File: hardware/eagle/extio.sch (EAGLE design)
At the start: 46 parts, among them IC1 PCF8574P, Q1 IRLZ44N, Q2 IRLZ44N, Q3 IRLZ44N, Q4 IRLZ44N, Q5 IRLZ44N, Q6 IRLZ44N, Q7 IRLZ44N, Q8 IRLZ44N

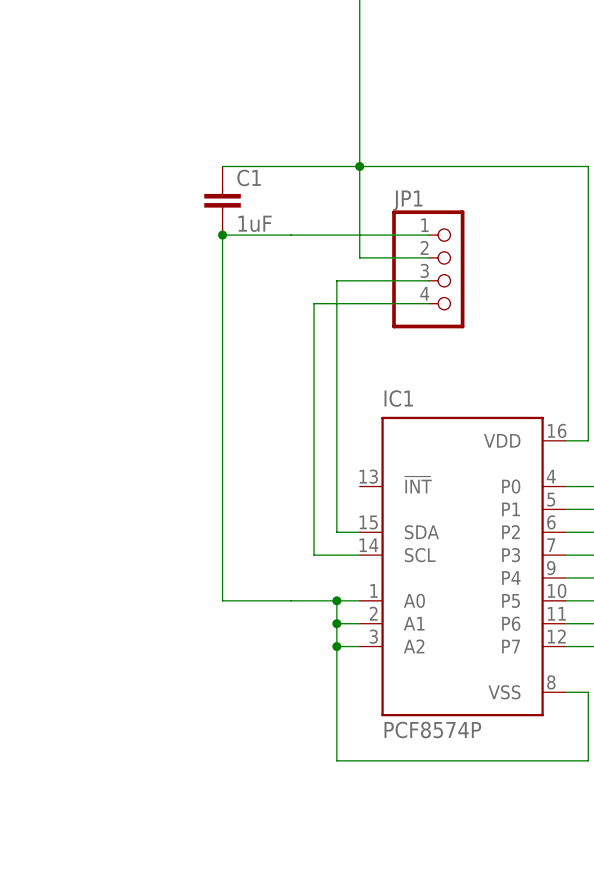
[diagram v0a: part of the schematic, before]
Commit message: ExtIO A0..A1: jmp1..jmp2
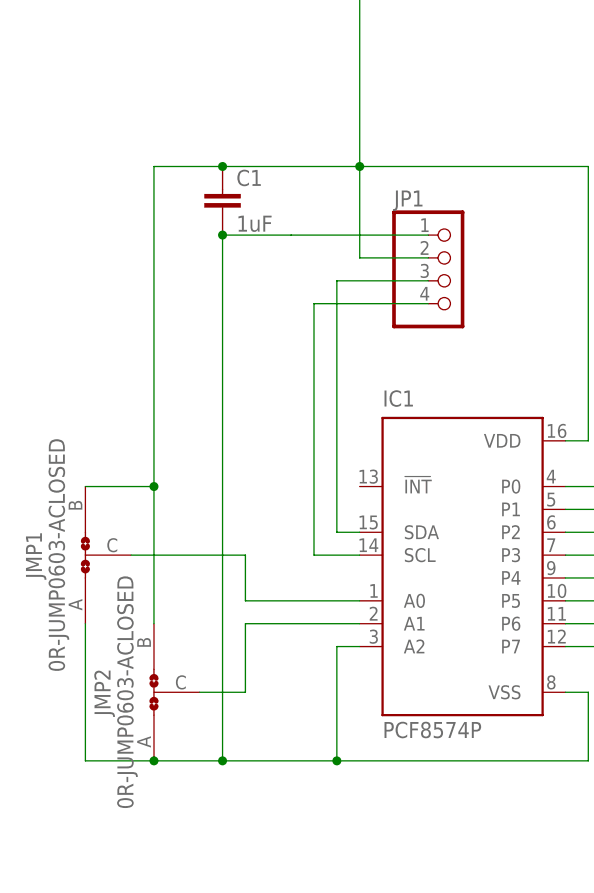
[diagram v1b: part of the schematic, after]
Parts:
- added JMP1, JMP2: 0R-JUMP0603-ACLOSED, gate433:0R-JUMP0603-ACLOSED
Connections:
- removed net N$71: C1.2, IC1.A0, IC1.A1, IC1.A2, IC1.VSS, JP1.1
- new net N$1: C1.2, IC1.A2, IC1.VSS, JMP1.A, JMP2.A, JP1.1
- new net N$2: IC1.A0, JMP1.C
- new net N$3: IC1.A1, JMP2.C
- net N$69: now also JMP1.B, JMP2.B
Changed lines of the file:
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@@
 <part name="D8" library="gate433" deviceset="ZENER-DIODE" device="SOD80C"/>
 <part name="C1" library="resistor" deviceset="C-EU" device="C0603" value="1uF"/>
+<part name="JMP1" library="gate433" deviceset="0R-JUMP" device="0603-ACLOSED"/>
+<part name="JMP2" library="gate433" deviceset="0R-JUMP" device="0603-ACLOSED"/>
 </parts>
 <sheets>
@@
 <instance part="D8" gate="G$1" x="170.18" y="17.78" rot="R90"/>
 <instance part="C1" gate="G$1" x="-5.08" y="83.82"/>
+<instance part="JMP1" gate="-0R" x="-20.32" y="43.18" rot="R90"/>
+<instance part="JMP2" gate="-0R" x="-12.7" y="27.94" rot="R90"/>
 </instances>
 <busses>
@@
 <pinref part="C1" gate="G$1" pin="1"/>
 <wire x1="-5.08" y1="86.36" x2="10.16" y2="86.36" width="0.1524" layer="91"/>
-</segment>
-</net>
-<net name="N$71" class="0">
-<segment>
-<pinref part="IC1" gate="G$1" pin="A0"/>
-<wire x1="10.16" y1="38.1" x2="7.62" y2="38.1" width="0.1524" layer="91"/>
-<wire x1="7.62" y1="38.1" x2="7.62" y2="35.56" width="0.1524" layer="91"/>
-<pinref part="IC1" gate="G$1" pin="A1"/>
-<wire x1="7.62" y1="35.56" x2="7.62" y2="33.02" width="0.1524" layer="91"/>
-<wire x1="10.16" y1="35.56" x2="7.62" y2="35.56" width="0.1524" layer="91"/>
-<junction x="7.62" y="35.56"/>
+<pinref part="JMP2" gate="-0R" pin="B"/>
+<wire x1="-12.7" y1="35.56" x2="-12.7" y2="50.8" width="0.1524" layer="91"/>
+<wire x1="-12.7" y1="50.8" x2="-12.7" y2="86.36" width="0.1524" layer="91"/>
+<wire x1="-12.7" y1="86.36" x2="-5.08" y2="86.36" width="0.1524" layer="91"/>
+<junction x="-5.08" y="86.36"/>
+<pinref part="JMP1" gate="-0R" pin="B"/>
+<wire x1="-20.32" y1="50.8" x2="-12.7" y2="50.8" width="0.1524" layer="91"/>
+<junction x="-12.7" y="50.8"/>
+</segment>
+</net>
+<net name="N$1" class="0">
+<segment>
+<pinref part="C1" gate="G$1" pin="2"/>
+<pinref part="JP1" gate="A" pin="1"/>
+<wire x1="2.54" y1="78.74" x2="17.78" y2="78.74" width="0.1524" layer="91"/>
+<wire x1="2.54" y1="78.74" x2="-5.08" y2="78.74" width="0.1524" layer="91"/>
 <pinref part="IC1" gate="G$1" pin="A2"/>
 <wire x1="10.16" y1="33.02" x2="7.62" y2="33.02" width="0.1524" layer="91"/>
@@
 <wire x1="35.56" y1="20.32" x2="7.62" y2="20.32" width="0.1524" layer="91"/>
 <wire x1="7.62" y1="20.32" x2="7.62" y2="33.02" width="0.1524" layer="91"/>
-<junction x="7.62" y="33.02"/>
-<wire x1="7.62" y1="38.1" x2="2.54" y2="38.1" width="0.1524" layer="91"/>
-<junction x="7.62" y="38.1"/>
-<pinref part="JP1" gate="A" pin="1"/>
-<wire x1="2.54" y1="78.74" x2="17.78" y2="78.74" width="0.1524" layer="91"/>
-<pinref part="C1" gate="G$1" pin="2"/>
-<wire x1="-5.08" y1="78.74" x2="-5.08" y2="38.1" width="0.1524" layer="91"/>
-<wire x1="-5.08" y1="38.1" x2="2.54" y2="38.1" width="0.1524" layer="91"/>
-<wire x1="2.54" y1="78.74" x2="-5.08" y2="78.74" width="0.1524" layer="91"/>
+<pinref part="JMP2" gate="-0R" pin="A"/>
+<wire x1="-12.7" y1="20.32" x2="-5.08" y2="20.32" width="0.1524" layer="91"/>
+<junction x="7.62" y="20.32"/>
+<pinref part="JMP1" gate="-0R" pin="A"/>
+<wire x1="-5.08" y1="20.32" x2="7.62" y2="20.32" width="0.1524" layer="91"/>
+<wire x1="-20.32" y1="35.56" x2="-20.32" y2="20.32" width="0.1524" layer="91"/>
+<wire x1="-20.32" y1="20.32" x2="-12.7" y2="20.32" width="0.1524" layer="91"/>
+<junction x="-12.7" y="20.32"/>
+<wire x1="-5.08" y1="78.74" x2="-5.08" y2="20.32" width="0.1524" layer="91"/>
 <junction x="-5.08" y="78.74"/>
-</segment>
-</net>
+<junction x="-5.08" y="20.32"/>
+</segment>
+</net>
+<net name="N$2" class="0">
+<segment>
+<pinref part="JMP1" gate="-0R" pin="C"/>
+<wire x1="-15.24" y1="43.18" x2="-2.54" y2="43.18" width="0.1524" layer="91"/>
+<wire x1="-2.54" y1="43.18" x2="-2.54" y2="38.1" width="0.1524" layer="91"/>
+<pinref part="IC1" gate="G$1" pin="A0"/>
+<wire x1="-2.54" y1="38.1" x2="10.16" y2="38.1" width="0.1524" layer="91"/>
+</segment>
+</net>
+<net name="N$3" class="0">
+<segment>
+<pinref part="JMP2" gate="-0R" pin="C"/>
+<wire x1="-7.62" y1="27.94" x2="-2.54" y2="27.94" width="0.1524" layer="91"/>
+<wire x1="-2.54" y1="27.94" x2="-2.54" y2="35.56" width="0.1524" layer="91"/>
+<pinref part="IC1" gate="G$1" pin="A1"/>
+<wire x1="-2.54" y1="35.56" x2="10.16" y2="35.56" width="0.1524" layer="91"/>
+</segment>
+</net>

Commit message: ExtIO: GND fix, JP1 via via :)
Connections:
- net N$1 renamed GND
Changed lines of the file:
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@@
 </segment>
 </net>
-<net name="N$1" class="0">
+<net name="GND" class="0">
 <segment>
 <pinref part="C1" gate="G$1" pin="2"/>
